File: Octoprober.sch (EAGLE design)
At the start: 140 parts, among them J1 10118193-0001LF, J2 26-60-4020, SW1 101-0134-EV, SW2 EVQ-Q2203W, SW3 EVQ-Q2203W, SW4 EVQ-Q2203W, SW5 EVQ-Q2203W, U1 P8X32A-M44, U10 MAX31855KASA+, U11 MAX31855KASA+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

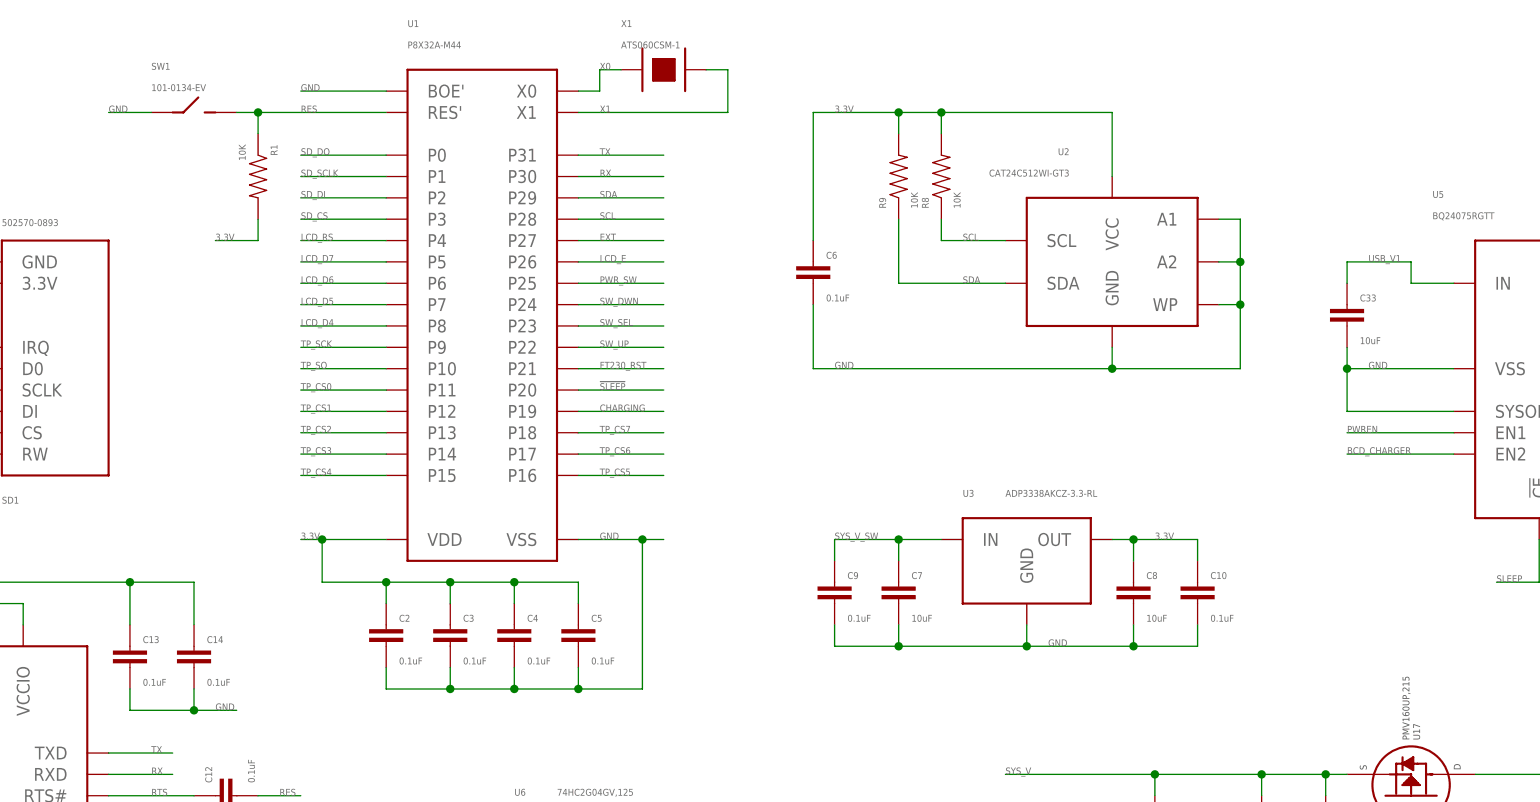
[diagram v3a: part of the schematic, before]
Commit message: Fixed screw terminal footprints.
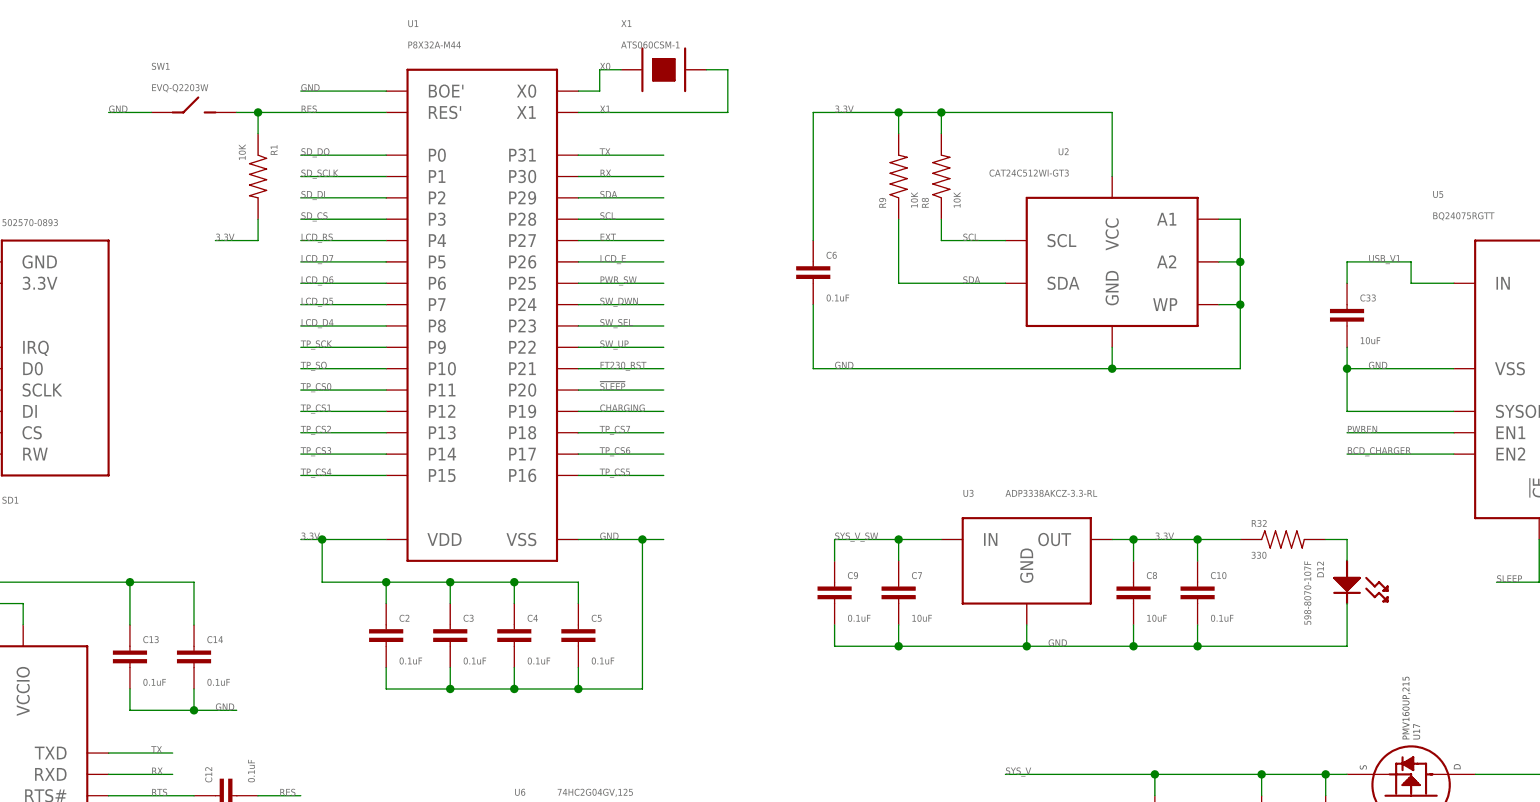
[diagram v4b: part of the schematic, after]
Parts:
- added D12: 598-8070-107F, PP_LED:LED_SINGLE0402
- added R32: 330, PP_Passives:RESISTOR0402
- SW1: value 101-0134-EV -> EVQ-Q2203W; device PP_Electromechanical:SPST101-0134-EV -> PP_Electromechanical:SPSTEVQ-Q2203W
- TC1, TC2, TC3, TC4, TC5, TC6, TC7, TC8: device PP_Connectors:PH_1X02HEADER_PTH -> PP_Connectors:PH_1X02SCREW_TERM
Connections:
- new net N$22: D12.ANODE, R32.2
- net 3.3V: now also R32.1
- net GND: now also D12.CATHODE

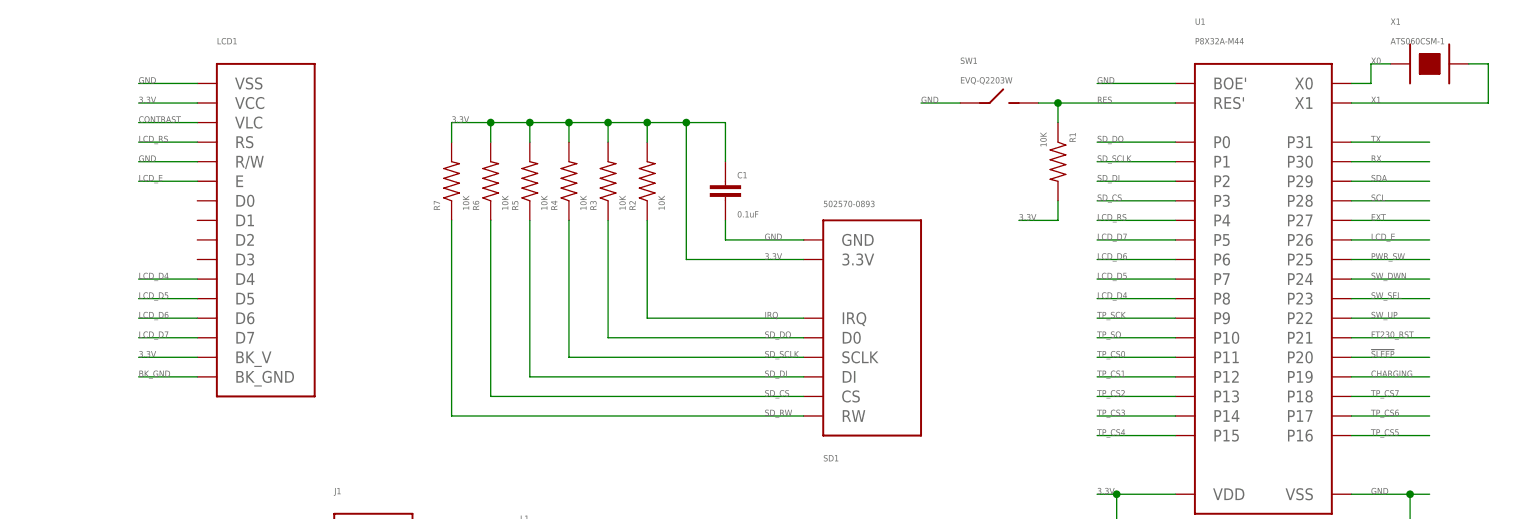
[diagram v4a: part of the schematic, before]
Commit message: LCD Screen is Serial now.
Wrote spin code for Serial interface.
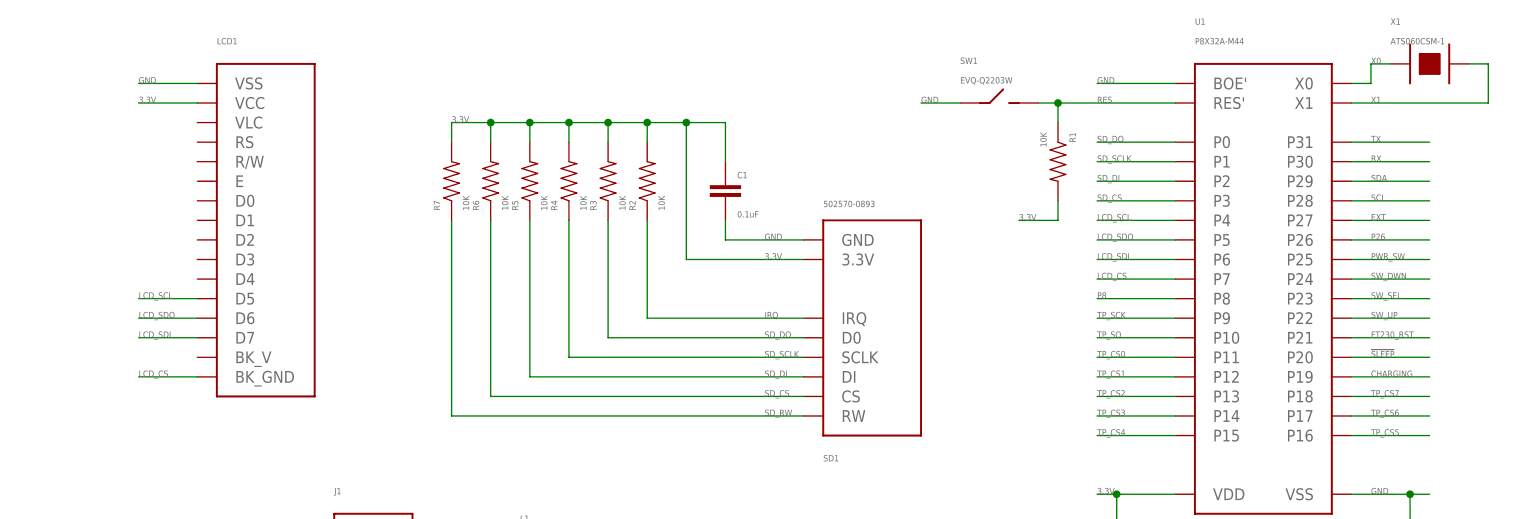
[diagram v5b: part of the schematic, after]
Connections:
- removed net BK_GND: LCD1.BK_GND
- removed net CONTRAST: LCD1.VLC
- removed net LCD_D4: LCD1.D4, U1.P8
- removed net LCD_D5: LCD1.D5, U1.P7
- removed net LCD_D6: LCD1.D6, U1.P6
- removed net LCD_D7: LCD1.D7, U1.P5
- removed net LCD_E: LCD1.E, U1.P26
- removed net LCD_RS: LCD1.RS, U1.P4
- new net LCD_CS: LCD1.BK_GND, U1.P7
- new net LCD_SCL: LCD1.D5, U1.P4
- new net LCD_SDI: LCD1.D7, U1.P6
- new net LCD_SDO: LCD1.D6, U1.P5
- new net P26: U1.P26
- new net P8: U1.P8
- net 3.3V: no longer LCD1.BK_V
- net GND: no longer LCD1.R/W

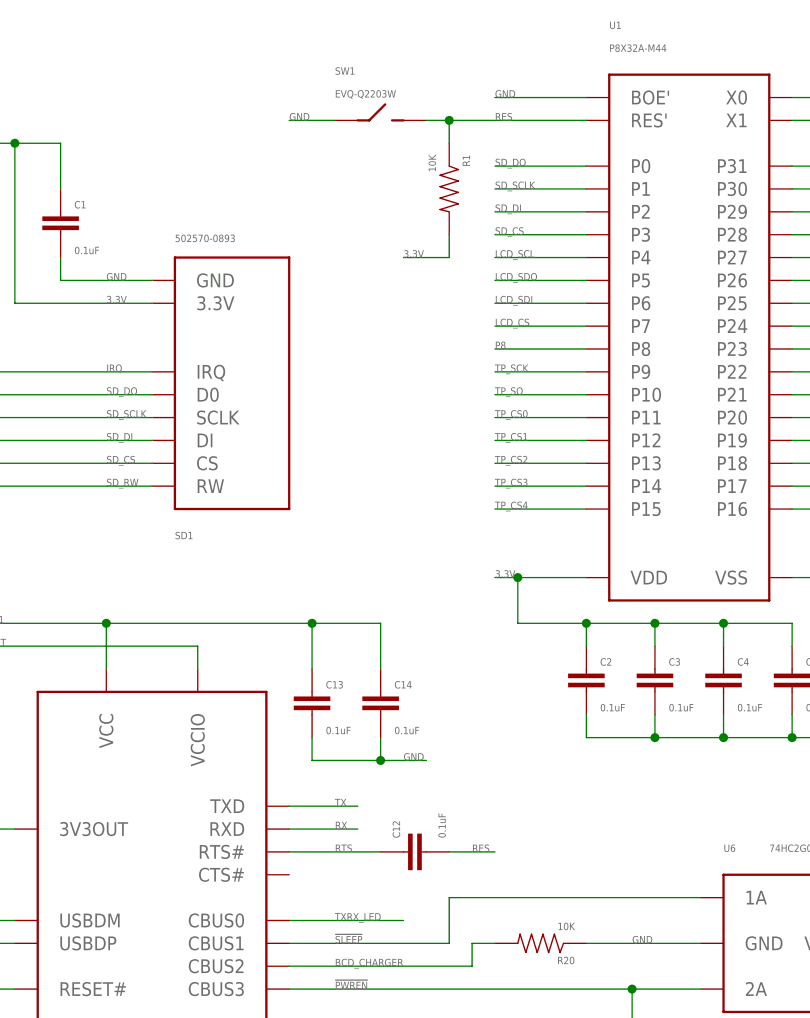
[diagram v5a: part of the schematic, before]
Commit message: Added code for Reset function.
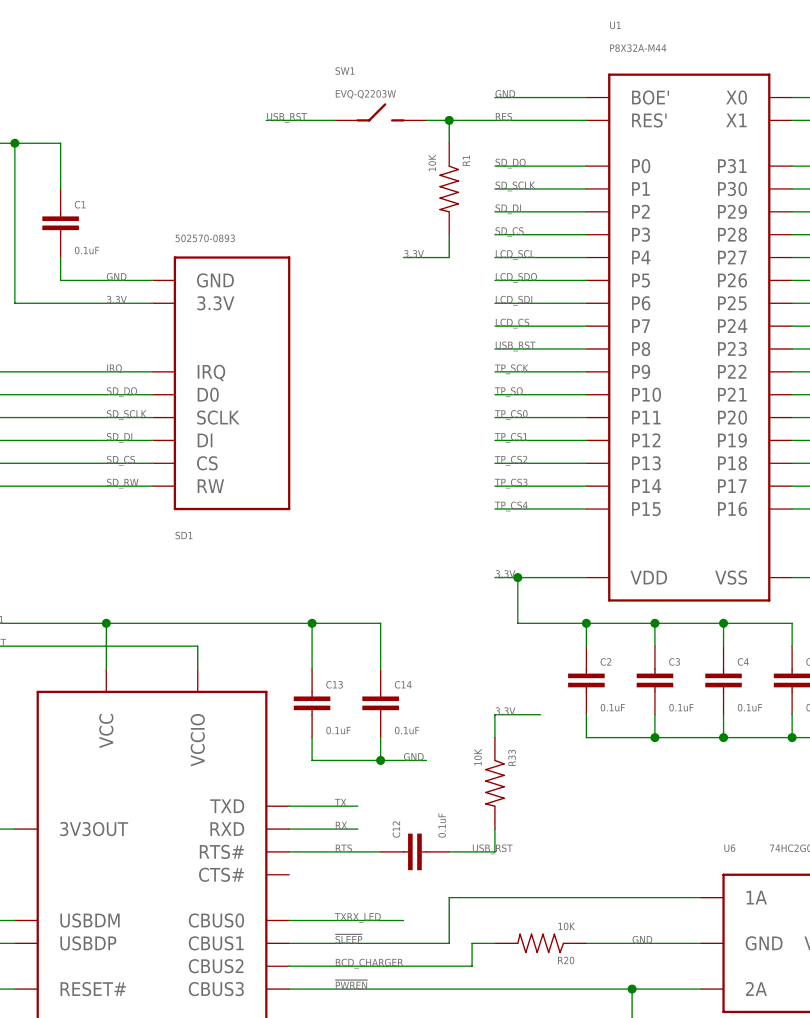
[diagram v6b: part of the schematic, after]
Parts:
- added R33: 10K, PP_Passives:RESISTOR0402
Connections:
- removed net P8: U1.P8
- new net USB_RST: C12.2, R33.2, SW1.A, U1.P8
- net 3.3V: now also R33.1
- net GND: no longer SW1.A
- net RES: no longer C12.2
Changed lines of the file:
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@@
 <part name="D12" library="PP_LED" deviceset="LED_SINGLE" device="0402" value="598-8070-107F"/>
 <part name="R32" library="PP_Passives" deviceset="RESISTOR" device="0402" value="330"/>
+<part name="R33" library="PP_Passives" deviceset="RESISTOR" device="0402" value="10K"/>
 </parts>
 <sheets>
@@
 <instance part="D12" gate="G$1" x="101.6" y="-27.94" rot="R270"/>
 <instance part="R32" gate="G$1" x="93.98" y="-22.86"/>
+<instance part="R33" gate="G$1" x="-22.86" y="-45.72" rot="R270"/>
 </instances>
 <busses>
@@
 <junction x="2.54" y="-40.64"/>
 <junction x="10.16" y="-40.64"/>
-</segment>
-<segment>
-<wire x1="-40.64" y1="27.94" x2="-45.72" y2="27.94" width="0.1524" layer="91"/>
-<label x="-45.72" y="27.94" size="0.8128" layer="95" font="vector"/>
-<pinref part="SW1" gate="G$1" pin="A"/>
 </segment>
 <segment>
@@
 <junction x="-27.94" y="27.94"/>
 <pinref part="SW1" gate="G$1" pin="B"/>
-</segment>
-<segment>
-<pinref part="C12" gate="G$1" pin="2"/>
-<wire x1="-27.94" y1="-53.34" x2="-22.86" y2="-53.34" width="0.1524" layer="91"/>
-<label x="-25.4" y="-53.34" size="0.8128" layer="95" font="vector"/>
 </segment>
 </net>
@@
 <label x="-93.98" y="-86.36" size="0.8128" layer="95" font="vector"/>
 </segment>
+<segment>
+<pinref part="R33" gate="G$1" pin="1"/>
+<wire x1="-22.86" y1="-40.64" x2="-22.86" y2="-38.1" width="0.1524" layer="91"/>
+<wire x1="-22.86" y1="-38.1" x2="-17.78" y2="-38.1" width="0.1524" layer="91"/>
+<label x="-22.86" y="-38.1" size="0.8128" layer="95" font="vector"/>
+</segment>
 </net>
 <net name="SD_RW" class="0">
@@
 </segment>
 </net>
-<net name="P8" class="0">
+<net name="USB_RST" class="0">
+<segment>
+<pinref part="C12" gate="G$1" pin="2"/>
+<wire x1="-27.94" y1="-53.34" x2="-22.86" y2="-53.34" width="0.1524" layer="91"/>
+<label x="-25.4" y="-53.34" size="0.8128" layer="95" font="vector"/>
+<pinref part="R33" gate="G$1" pin="2"/>
+<wire x1="-22.86" y1="-50.8" x2="-22.86" y2="-53.34" width="0.1524" layer="91"/>
+</segment>
+<segment>
+<wire x1="-40.64" y1="27.94" x2="-48.26" y2="27.94" width="0.1524" layer="91"/>
+<label x="-48.26" y="27.94" size="0.8128" layer="95" font="vector"/>
+<pinref part="SW1" gate="G$1" pin="A"/>
+</segment>
 <segment>
 <pinref part="U1" gate="G$1" pin="P8"/>
